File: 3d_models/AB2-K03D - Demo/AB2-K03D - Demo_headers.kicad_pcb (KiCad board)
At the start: 2 copper layers, 128 parts

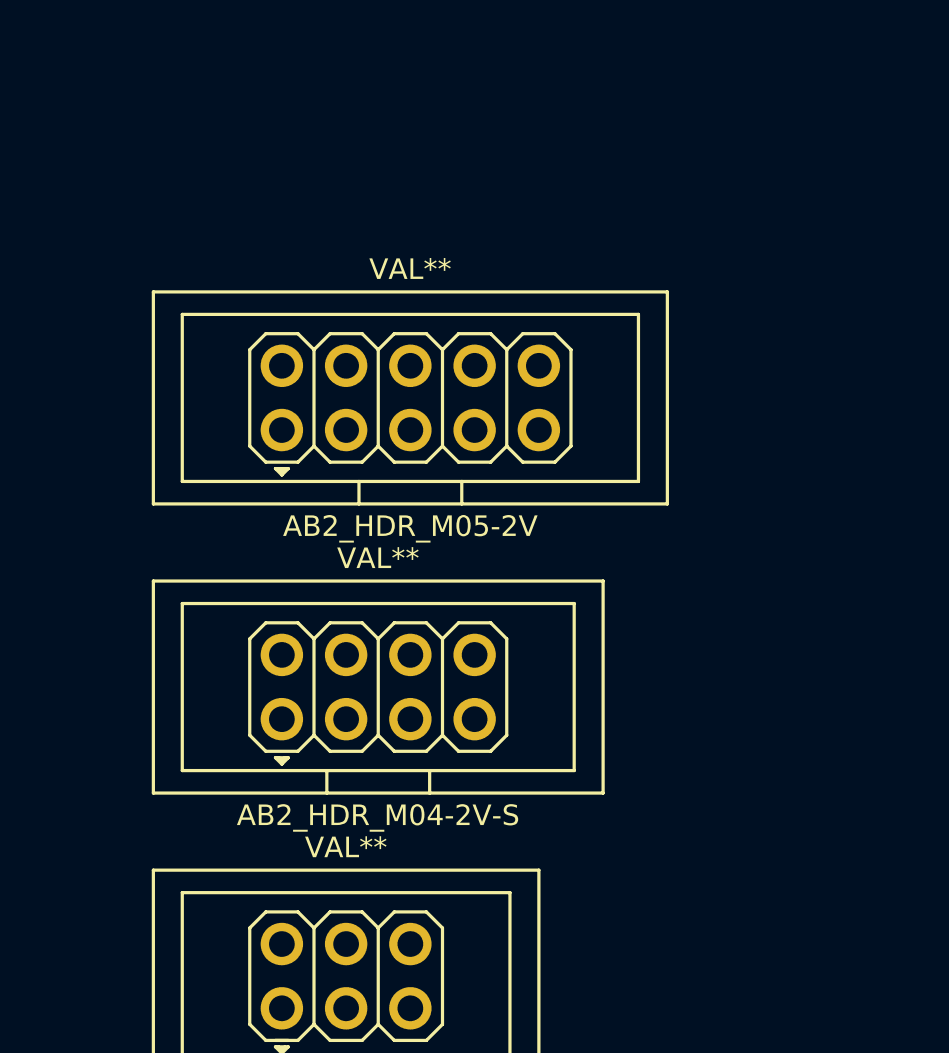
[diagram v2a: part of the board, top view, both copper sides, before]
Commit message: 3d: AB2-K03D: add 7pin idc shroud hdr
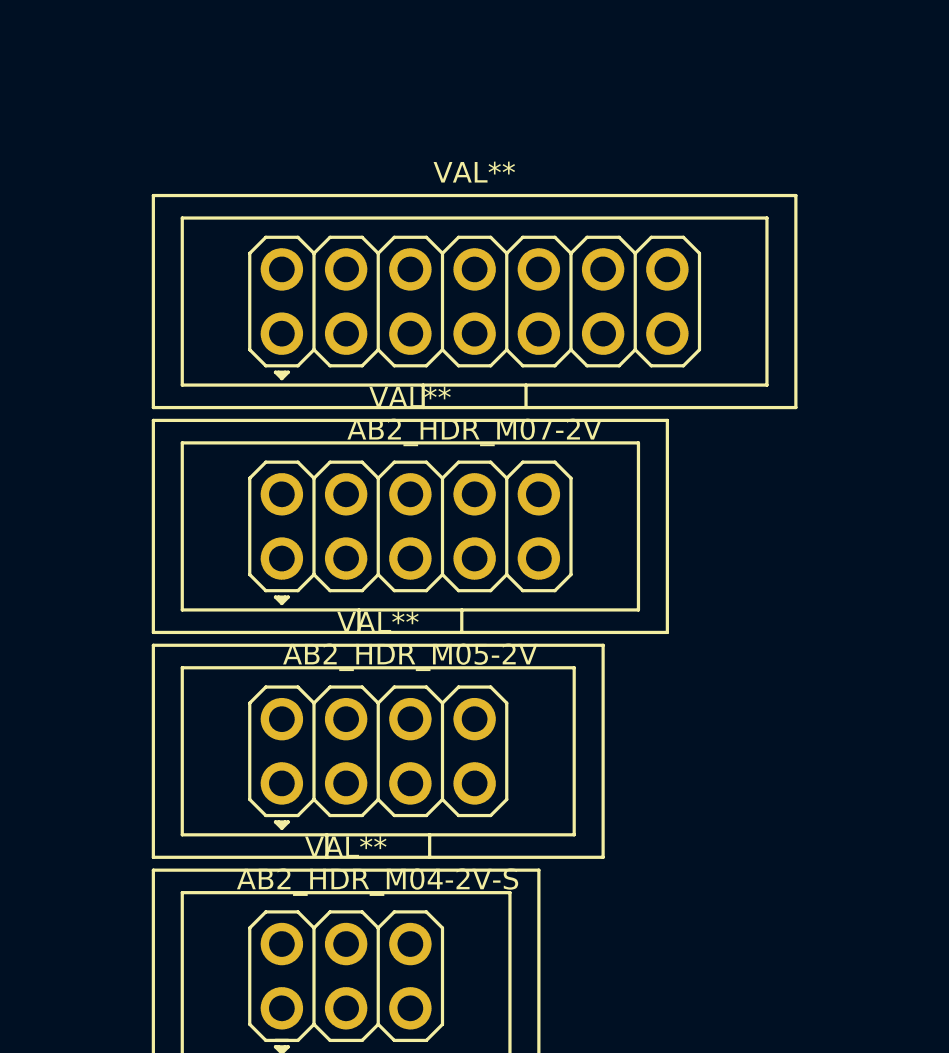
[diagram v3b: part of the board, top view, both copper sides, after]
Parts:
- added AB2_HDR_M07-2V: VAL**, AB2_HDR_M07-2V-S, F.Cu at (26.7, 252.7)
- moved AB2_HDR_M05-2V 5.08 mm to (24.1, 261.6)
- moved AB2_HDR_M04-2V-S 2.54 mm to (22.9, 270.5)
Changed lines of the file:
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@@
     (tracks 0)
     (zones 0)
-    (modules 128)
+    (modules 129)
     (nets 1)
   )
@@
   )
   (module AB2_HDR_M04-2V-S (layer F.Cu)
-    (at 22.86 267.97)
+    (at 22.86 270.51)
     (path AB2_HDR05_2)
     (fp_text reference AB2_HDR_M04-2V-S (at 0 5.08) (layer F.SilkS)
@@
   )
   (module AB2_HDR_M05-2V-S (layer F.Cu)
-    (at 24.13 256.54)
+    (at 24.13 261.62)
     (fp_text reference AB2_HDR_M05-2V (at 0 5.08) (layer F.SilkS)
       (effects (font (size 0.8128 0.8128) (thickness 0.0762)))
@@
       (at (xyz 0 0 0))
       (scale (xyz 0.3937 0.3937 0.3937))
+      (rotate (xyz 0 0 0))
+    )
+  )
+  (module AB2_HDR_M07-2V-S (layer F.Cu)
+    (at 26.67 252.73)
+    (path AB2_HDR07_2)
+    (fp_text reference AB2_HDR_M07-2V (at 0 5.08) (layer F.SilkS)
+      (effects (font (size 0.8128 0.8128) (thickness 0.0762)))
+    )
+    (fp_text value VAL** (at 0 -5.08) (layer F.SilkS)
+      (effects (font (size 0.8128 0.8128) (thickness 0.0762)))
+    )
+    (fp_line (start 2.032 3.302) (end 2.032 4.191) (layer F.SilkS) (width 0.127))
+    (fp_line (start -2.032 3.302) (end -2.032 4.191) (layer F.SilkS) (width 0.127))
+    (fp_line (start -7.493 2.794) (end -7.62 2.921) (layer F.SilkS) (width 0.127))
+    (fp_line (start -7.747 2.794) (end -7.62 2.921) (layer F.SilkS) (width 0.127))
+    (fp_line (start -7.874 2.794) (end -7.62 3.048) (layer F.SilkS) (width 0.127))
+    (fp_line (start -7.62 3.048) (end -7.366 2.794) (layer F.SilkS) (width 0.127))
+    (fp_line (start -7.366 2.794) (end -7.874 2.794) (layer F.SilkS) (width 0.127))
+    (fp_line (start 12.7 -4.191) (end 12.7 4.191) (layer F.SilkS) (width 0.127))
+    (fp_line (start 12.7 4.191) (end -12.7 4.191) (layer F.SilkS) (width 0.127))
+    (fp_line (start -12.7 4.191) (end -12.7 -4.191) (layer F.SilkS) (width 0.127))
+    (fp_line (start -12.7 -4.191) (end 12.7 -4.191) (layer F.SilkS) (width 0.127))
+    (fp_line (start 11.557 -3.302) (end 11.557 3.302) (layer F.SilkS) (width 0.127))
+    (fp_line (start -11.557 -3.302) (end -11.557 3.302) (layer F.SilkS) (width 0.127))
+    (fp_line (start 11.557 3.302) (end -11.557 3.302) (layer F.SilkS) (width 0.127))
+    (fp_line (start -11.557 -3.302) (end 11.557 -3.302) (layer F.SilkS) (width 0.127))
+    (fp_line (start 6.35 -1.905) (end 6.985 -2.54) (layer F.SilkS) (width 0.127))
+    (fp_line (start 6.985 -2.54) (end 8.255 -2.54) (layer F.SilkS) (width 0.127))
+    (fp_line (start 8.255 -2.54) (end 8.89 -1.905) (layer F.SilkS) (width 0.127))
+    (fp_line (start 8.89 -1.905) (end 8.89 1.905) (layer F.SilkS) (width 0.127))
+    (fp_line (start 8.89 1.905) (end 8.255 2.54) (layer F.SilkS) (width 0.127))
+    (fp_line (start 8.255 2.54) (end 6.985 2.54) (layer F.SilkS) (width 0.127))
+    (fp_line (start 6.985 2.54) (end 6.35 1.905) (layer F.SilkS) (width 0.127))
+    (fp_line (start 3.81 -1.905) (end 4.445 -2.54) (layer F.SilkS) (width 0.127))
+    (fp_line (start 4.445 -2.54) (end 5.715 -2.54) (layer F.SilkS) (width 0.127))
+    (fp_line (start 5.715 -2.54) (end 6.35 -1.905) (layer F.SilkS) (width 0.127))
+    (fp_line (start 6.35 -1.905) (end 6.35 1.905) (layer F.SilkS) (width 0.127))
+    (fp_line (start 6.35 1.905) (end 5.715 2.54) (layer F.SilkS) (width 0.127))
+    (fp_line (start 5.715 2.54) (end 4.445 2.54) (layer F.SilkS) (width 0.127))
+    (fp_line (start 4.445 2.54) (end 3.81 1.905) (layer F.SilkS) (width 0.127))
+    (fp_line (start 1.27 -1.905) (end 1.905 -2.54) (layer F.SilkS) (width 0.127))
+    (fp_line (start 1.905 -2.54) (end 3.175 -2.54) (layer F.SilkS) (width 0.127))
+    (fp_line (start 3.175 -2.54) (end 3.81 -1.905) (layer F.SilkS) (width 0.127))
+    (fp_line (start 3.81 -1.905) (end 3.81 1.905) (layer F.SilkS) (width 0.127))
+    (fp_line (start 3.81 1.905) (end 3.175 2.54) (layer F.SilkS) (width 0.127))
+    (fp_line (start 3.175 2.54) (end 1.905 2.54) (layer F.SilkS) (width 0.127))
+    (fp_line (start 1.905 2.54) (end 1.27 1.905) (layer F.SilkS) (width 0.127))
+    (fp_line (start -1.27 -1.905) (end -0.635 -2.54) (layer F.SilkS) (width 0.127))
+    (fp_line (start -0.635 -2.54) (end 0.635 -2.54) (layer F.SilkS) (width 0.127))
+    (fp_line (start 0.635 -2.54) (end 1.27 -1.905) (layer F.SilkS) (width 0.127))
+    (fp_line (start 1.27 -1.905) (end 1.27 1.905) (layer F.SilkS) (width 0.127))
+    (fp_line (start 1.27 1.905) (end 0.635 2.54) (layer F.SilkS) (width 0.127))
+    (fp_line (start 0.635 2.54) (end -0.635 2.54) (layer F.SilkS) (width 0.127))
+    (fp_line (start -0.635 2.54) (end -1.27 1.905) (layer F.SilkS) (width 0.127))
+    (fp_line (start -3.81 -1.905) (end -3.175 -2.54) (layer F.SilkS) (width 0.127))
+    (fp_line (start -3.175 -2.54) (end -1.905 -2.54) (layer F.SilkS) (width 0.127))
+    (fp_line (start -1.905 -2.54) (end -1.27 -1.905) (layer F.SilkS) (width 0.127))
+    (fp_line (start -1.27 -1.905) (end -1.27 1.905) (layer F.SilkS) (width 0.127))
+    (fp_line (start -1.27 1.905) (end -1.905 2.54) (layer F.SilkS) (width 0.127))
+    (fp_line (start -1.905 2.54) (end -3.175 2.54) (layer F.SilkS) (width 0.127))
+    (fp_line (start -3.175 2.54) (end -3.81 1.905) (layer F.SilkS) (width 0.127))
+    (fp_line (start -6.35 -1.905) (end -5.715 -2.54) (layer F.SilkS) (width 0.127))
+    (fp_line (start -5.715 -2.54) (end -4.445 -2.54) (layer F.SilkS) (width 0.127))
+    (fp_line (start -4.445 -2.54) (end -3.81 -1.905) (layer F.SilkS) (width 0.127))
+    (fp_line (start -3.81 -1.905) (end -3.81 1.905) (layer F.SilkS) (width 0.127))
+    (fp_line (start -3.81 1.905) (end -4.445 2.54) (layer F.SilkS) (width 0.127))
+    (fp_line (start -4.445 2.54) (end -5.715 2.54) (layer F.SilkS) (width 0.127))
+    (fp_line (start -5.715 2.54) (end -6.35 1.905) (layer F.SilkS) (width 0.127))
+    (fp_line (start -8.255 2.54) (end -8.89 1.905) (layer F.SilkS) (width 0.127))
+    (fp_line (start -8.89 1.905) (end -8.89 -1.905) (layer F.SilkS) (width 0.127))
+    (fp_line (start -8.89 -1.905) (end -8.255 -2.54) (layer F.SilkS) (width 0.127))
+    (fp_line (start -8.255 -2.54) (end -6.985 -2.54) (layer F.SilkS) (width 0.127))
+    (fp_line (start -6.985 -2.54) (end -6.35 -1.905) (layer F.SilkS) (width 0.127))
+    (fp_line (start -6.35 -1.905) (end -6.35 1.905) (layer F.SilkS) (width 0.127))
+    (fp_line (start -6.35 1.905) (end -6.985 2.54) (layer F.SilkS) (width 0.127))
+    (fp_line (start -6.985 2.54) (end -8.255 2.54) (layer F.SilkS) (width 0.127))
+    (pad 1 thru_hole circle (at -7.62 1.27) (size 1.6764 1.6764) (drill 1.016)
+      (layers *.Cu *.Mask F.SilkS)
+    )
+    (pad 2 thru_hole circle (at -7.62 -1.27) (size 1.6764 1.6764) (drill 1.016)
+      (layers *.Cu *.Mask F.SilkS)
+    )
+    (pad 3 thru_hole circle (at -5.08 1.27) (size 1.6764 1.6764) (drill 1.016)
+      (layers *.Cu *.Mask F.SilkS)
+    )
+    (pad 4 thru_hole circle (at -5.08 -1.27) (size 1.6764 1.6764) (drill 1.016)
+      (layers *.Cu *.Mask F.SilkS)
+    )
+    (pad 5 thru_hole circle (at -2.54 1.27) (size 1.6764 1.6764) (drill 1.016)
+      (layers *.Cu *.Mask F.SilkS)
+    )
+    (pad 6 thru_hole circle (at -2.54 -1.27) (size 1.6764 1.6764) (drill 1.016)
+      (layers *.Cu *.Mask F.SilkS)
+    )
+    (pad 7 thru_hole circle (at 0 1.27) (size 1.6764 1.6764) (drill 1.016)
+      (layers *.Cu *.Mask F.SilkS)
+    )
+    (pad 8 thru_hole circle (at 0 -1.27) (size 1.6764 1.6764) (drill 1.016)
+      (layers *.Cu *.Mask F.SilkS)
+    )
+    (pad 9 thru_hole circle (at 2.54 1.27) (size 1.6764 1.6764) (drill 1.016)
+      (layers *.Cu *.Mask F.SilkS)
+    )
+    (pad 10 thru_hole circle (at 2.54 -1.27) (size 1.6764 1.6764) (drill 1.016)
+      (layers *.Cu *.Mask F.SilkS)
+    )
+    (pad 11 thru_hole circle (at 5.08 1.27) (size 1.6764 1.6764) (drill 1.016)
+      (layers *.Cu *.Mask F.SilkS)
+    )
+    (pad 12 thru_hole circle (at 5.08 -1.27) (size 1.6764 1.6764) (drill 1.016)
+      (layers *.Cu *.Mask F.SilkS)
+    )
+    (pad 13 thru_hole circle (at 7.62 1.27) (size 1.6764 1.6764) (drill 1.016)
+      (layers *.Cu *.Mask F.SilkS)
+    )
+    (pad 14 thru_hole circle (at 7.62 -1.27) (size 1.6764 1.6764) (drill 1.016)
+      (layers *.Cu *.Mask F.SilkS)
+    )
+    (model ../3d_models/ab2_idc/AB2_HDR_M07-2V-S-3M.wrl
+      (at (xyz 0 0 0))
+      (scale (xyz 0.3937 0.3937 0.3937))
